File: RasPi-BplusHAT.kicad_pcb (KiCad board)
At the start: 2 copper layers, 65 x 56 mm, 11 parts, among them K1 PIN20X2, U1 EEPROM24

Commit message: Fix zones
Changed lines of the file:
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@@
     (links 26)
     (no_connects 26)
-    (area 114.665415 76.924999 182.336786 133.075001)
+    (area 115.924999 76.924999 181.075001 133.075001)
     (thickness 1.6)
     (drawings 23)
@@
   (page A4)
   (layers
-    (0 Top signal hide)
-    (31 Bottom signal hide)
+    (0 Top signal)
+    (31 Bottom signal)
     (32 B.Adhes user)
     (33 F.Adhes user)
@@
     (42 Eco1.User user)
     (43 Eco2.User user)
-    (44 Edge.Cuts user)
+    (44 Edge.Cuts user hide)
     (45 Margin user)
     (46 B.CrtYd user)
@@
     (connect_pads (clearance 0.508))
     (min_thickness 0.254)
-    (fill (arc_segments 32) (thermal_gap 0.508) (thermal_bridge_width 0.508))
+    (fill yes (arc_segments 32) (thermal_gap 0.508) (thermal_bridge_width 0.508))
     (polygon
       (pts
-        (xy 116.0011 130.0036) (xy 119.0011 133.0036) (xy 178.0011 133.0036) (xy 181.0011 130.0036) (xy 181.0011 80.0036)
-        (xy 178.0011 77.0036) (xy 119.0011 77.0036) (xy 116.0011 80.0036) (xy 116.0011 95.5036) (xy 117.0011 96.5036)
+        (xy 116.0011 130.0036) (xy 116 133) (xy 178.0011 133.0036) (xy 181 133) (xy 181.0011 80.0036)
+        (xy 181 77) (xy 116 77) (xy 116.0011 80.0036) (xy 116.0011 95.5036) (xy 117.0011 96.5036)
         (xy 120.0011 96.5036) (xy 121.0011 97.5036) (xy 121.0011 112.5036) (xy 120.0011 113.5036) (xy 117.0011 113.5036)
         (xy 116.0011 114.5036)
@@
     (connect_pads (clearance 0.508))
     (min_thickness 0.254)
-    (fill (arc_segments 32) (thermal_gap 0.508) (thermal_bridge_width 0.508))
+    (fill yes (arc_segments 32) (thermal_gap 0.508) (thermal_bridge_width 0.508))
     (polygon
       (pts
-        (xy 116.0011 130.0036) (xy 119.0011 133.0036) (xy 178.0011 133.0036) (xy 181.0011 130.0036) (xy 181.0011 80.0036)
-        (xy 178.0011 77.0036) (xy 119.0011 77.0036) (xy 116.0011 80.0036) (xy 116.0011 95.5036) (xy 117.0011 96.5036)
+        (xy 116 133) (xy 119.0011 133.0036) (xy 181 133) (xy 181 130) (xy 181 77)
+        (xy 178.0011 77.0036) (xy 119.0011 77.0036) (xy 116 77) (xy 116.0011 95.5036) (xy 117.0011 96.5036)
         (xy 120.0011 96.5036) (xy 121.0011 97.5036) (xy 121.0011 112.5036) (xy 120.0011 113.5036) (xy 117.0011 113.5036)
         (xy 116.0011 114.5036)

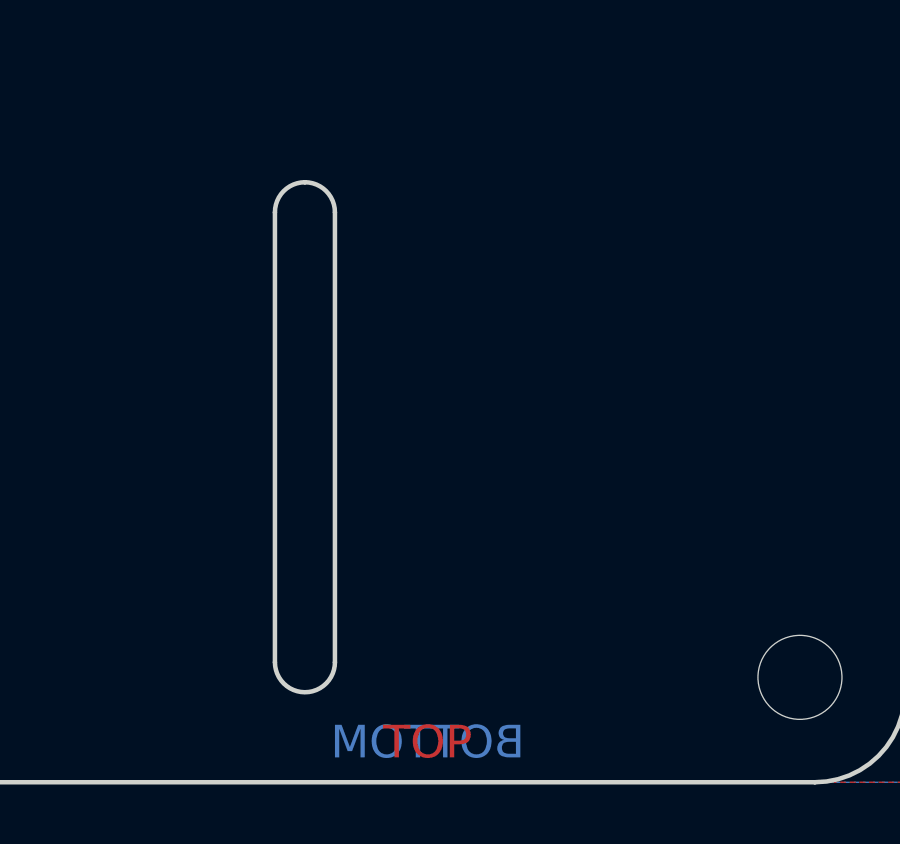
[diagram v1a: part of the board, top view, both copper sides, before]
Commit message: Update cam slot arc
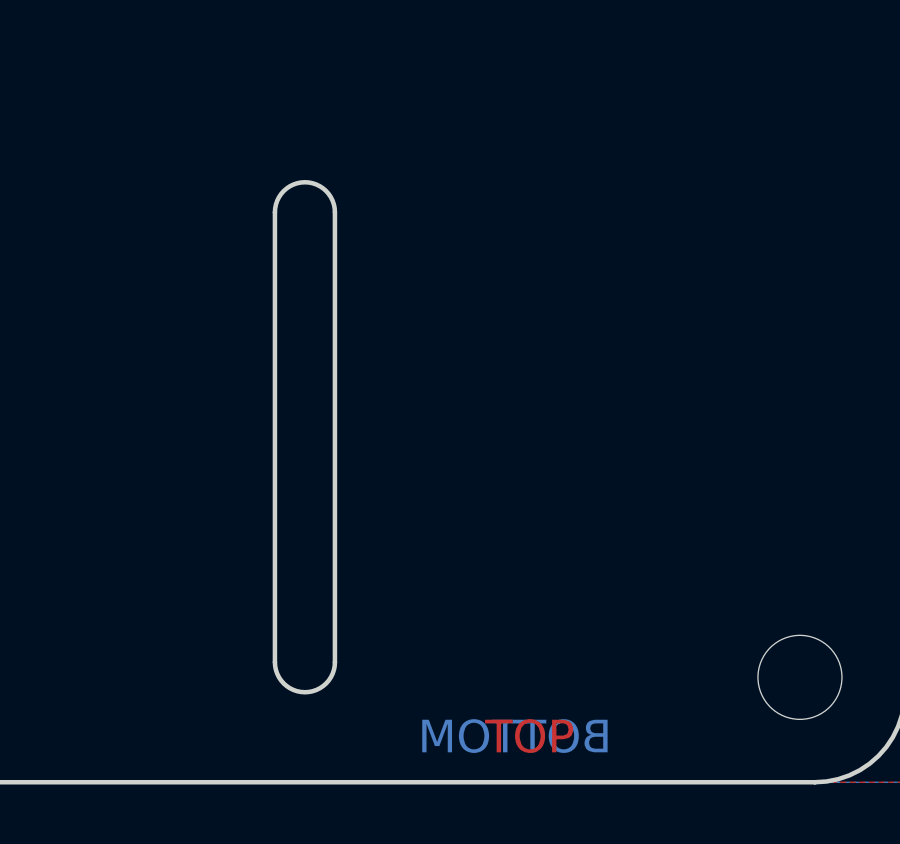
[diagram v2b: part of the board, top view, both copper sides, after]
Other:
- outline, holes or cut-outs redrawn
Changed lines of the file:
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@@
     (area 115.924999 76.924999 181.075001 133.075001)
     (thickness 1.6)
-    (drawings 23)
+    (drawings 22)
     (tracks 0)
     (zones 0)
@@
     (42 Eco1.User user)
     (43 Eco2.User user)
-    (44 Edge.Cuts user hide)
+    (44 Edge.Cuts user)
     (45 Margin user)
     (46 B.CrtYd user)
@@
       (net 1 GND))
   )
+  (gr_arc (start 161 114) (end 160 114) (angle 180) (layer Edge.Cuts) (width 0.15))
+  (gr_arc (start 161 129) (end 160 129) (angle -180) (layer Edge.Cuts) (width 0.15))
   (gr_arc (start 117 114.5) (end 117 113.5) (angle -90) (layer Edge.Cuts) (width 0.15))
   (gr_arc (start 120 112.5) (end 120 113.5) (angle -90) (layer Edge.Cuts) (width 0.15))
   (gr_arc (start 117 95.5) (end 116 95.5) (angle -90) (layer Edge.Cuts) (width 0.15))
   (gr_arc (start 120 97.5) (end 121 97.5) (angle -90) (layer Edge.Cuts) (width 0.15))
-  (gr_arc (start 161 129) (end 160 129) (angle -180) (layer Edge.Cuts) (width 0.15))
-  (gr_arc (start 161 114) (end 160 114) (angle 90) (layer Edge.Cuts) (width 0.15))
-  (gr_arc (start 161 114) (end 161 113) (angle 90) (layer Edge.Cuts) (width 0.15))
   (gr_arc (start 178 80) (end 181 80) (angle -90) (layer Edge.Cuts) (width 0.15))
   (gr_arc (start 178 130) (end 178 133) (angle -90) (layer Edge.Cuts) (width 0.15))
@@
   (gr_line (start 120 113.5) (end 117 113.5) (layer Edge.Cuts) (width 0.15))
   (gr_line (start 116 114.5) (end 116 130) (layer Edge.Cuts) (width 0.15))
-  (gr_text TOP (at 165.0911 131.6686) (layer Top)
+  (gr_text TOP (at 168.5 131.5) (layer Top)
     (effects (font (size 1.08585 1.08585) (thickness 0.26289)))
   )
-  (gr_text BOTTOM (at 165.0911 131.6686) (layer Bottom)
+  (gr_text BOTTOM (at 168 131.5) (layer Bottom)
     (effects (font (size 1.08585 1.08585) (thickness 0.26289)) (justify mirror))
   )
